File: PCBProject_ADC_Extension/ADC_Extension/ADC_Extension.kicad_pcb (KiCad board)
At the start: 2 copper layers, 279 parts, among them J1 Conn_01x20, J10 Conn_01x02, J11 Conn_01x02, J12 Conn_01x02, J13 Conn_01x02, J14 Conn_01x02, J15 Conn_01x02, J2 Conn_01x02, J3 Conn_01x02, J4 Conn_01x02, J5 Conn_01x02, J6 Conn_01x02, J7 Conn_01x02, J8 Conn_01x02, J9 Conn_01x02

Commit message: 布局50%请求援助
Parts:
- moved J11 8.34 mm to (67.0, 146.7), turned to -90 degrees
- moved J2 8.17 mm to (66.8, 77.7), turned to -90 degrees
- moved J15 7.18 mm to (118.0, 146.6), turned to -90 degrees
- moved J1 6.10 mm to (48.2, 86.9)
- moved ANALOGINPUT7 4.98 mm to (133.8, 108.3)
- moved C77 4.98 mm to (135.4, 130.3)
- moved C78 4.98 mm to (135.3, 126.8)
- moved D15 4.98 mm to (134.1, 119.4)
- moved D8 4.98 mm to (134.1, 104.8)
- moved R128 4.98 mm to (138.1, 122.4)
- moved R129 4.98 mm to (133.6, 133.7)
- moved R130 4.98 mm to (135.3, 123.2)
- moved R132 4.98 mm to (138.2, 127.4)
- moved R55 4.98 mm to (138.3, 102.3)
- moved R59 4.98 mm to (138.1, 97.2)
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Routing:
- net /ADC5: track 7.22 -> 125.2 mm, vias 0 -> 2
- net /ADD3: track 7.18 -> 123.3 mm, vias 0 -> 2
- net /ADD4: track 7.21 -> 58.3 mm
- net /ADB4: track 7.22 -> 52.4 mm, vias 0 -> 1
- net /AD_15: track 7.18 -> 42.1 mm
- net /IN-_9: track 0.00 -> 33.8 mm
- net /IN-_7: track 0.00 -> 33.0 mm
- net /IN-_13: track 0.00 -> 32.4 mm
- net /IN-_6: track 0.00 -> 31.4 mm
- net /IN-_12: track 0.00 -> 30.9 mm
- net /IN-_2: track 0.00 -> 30.2 mm
- net /ADC4: track 7.13 -> 36.4 mm
- net /ADC3: track 7.18 -> 36.4 mm, vias 0 -> 1
- net /IN-_3: track 0.00 -> 29.1 mm
- net /ADB5: track 7.21 -> 36.0 mm, vias 0 -> 1
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- added copper zone on In1.Cu, net AGND
- added copper zone on In2.Cu, net AGND
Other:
- copper layers 2 -> 4

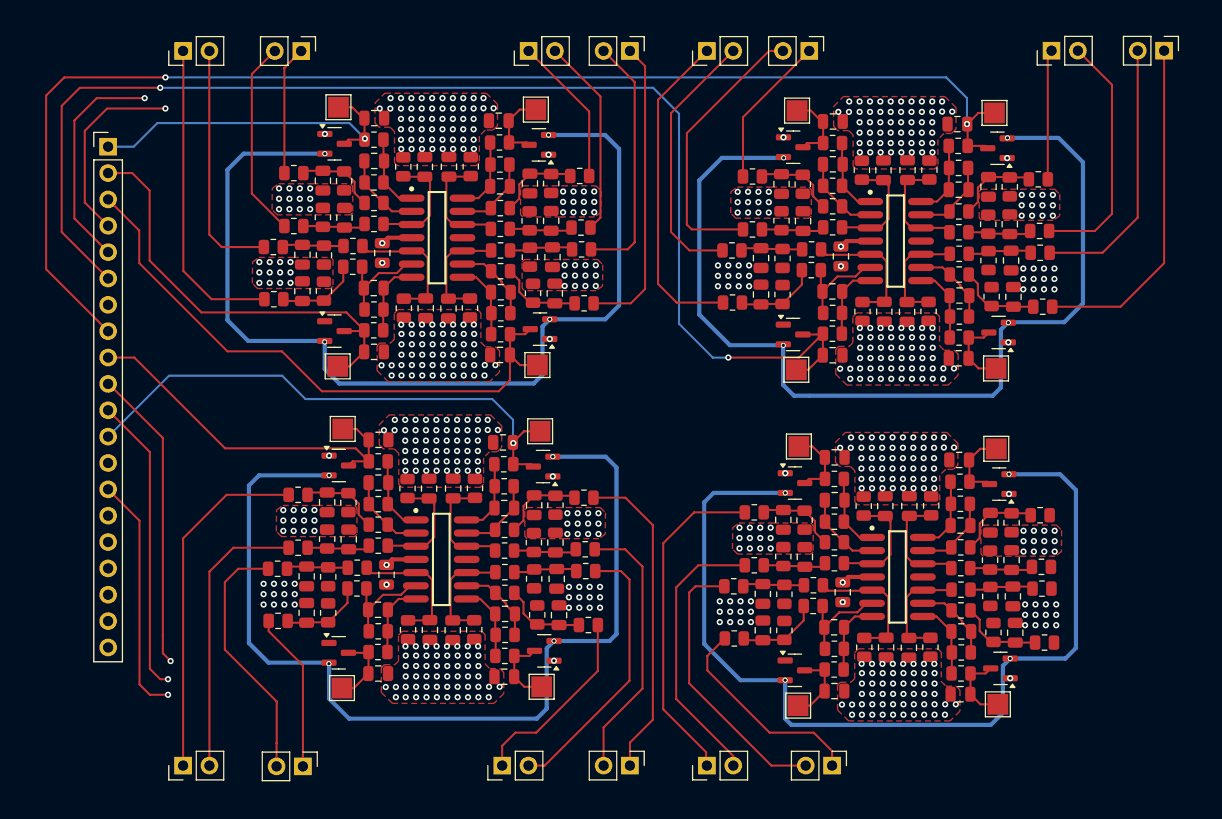
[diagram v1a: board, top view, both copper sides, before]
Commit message: 完成ADC拓展
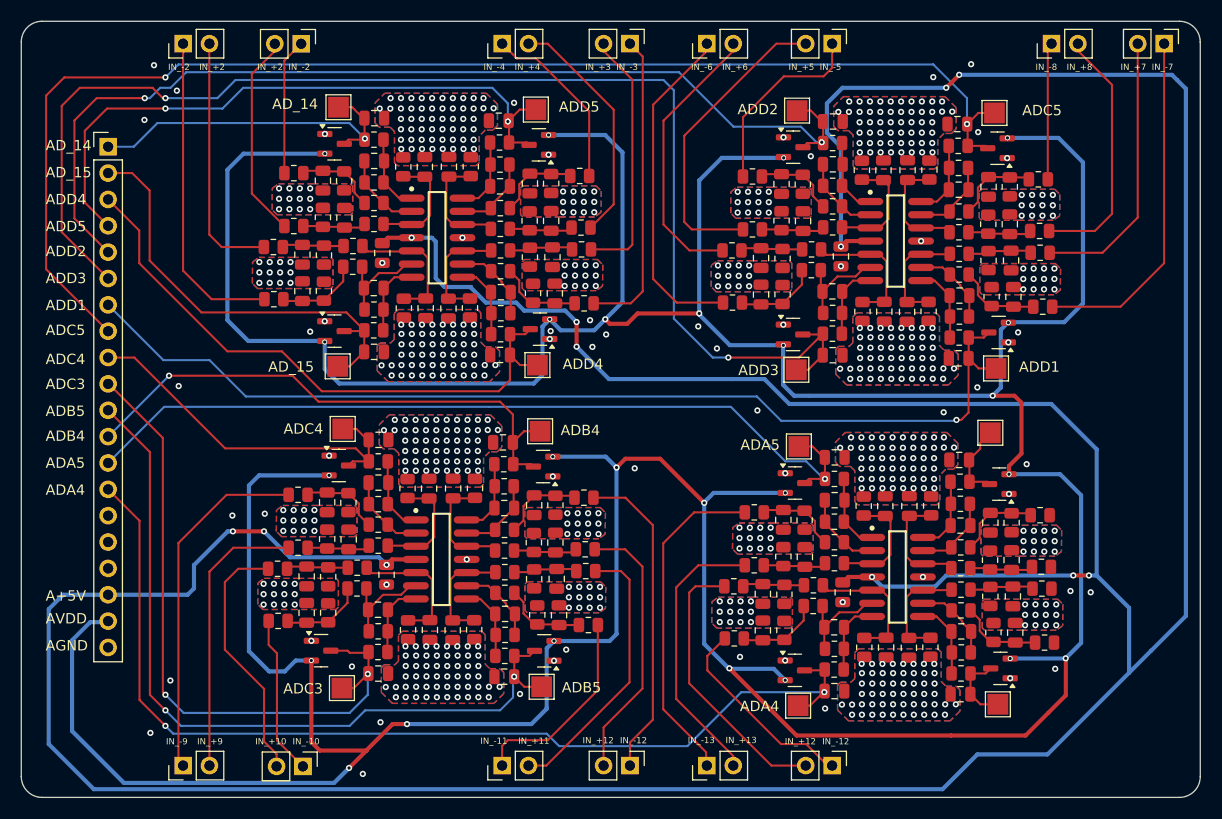
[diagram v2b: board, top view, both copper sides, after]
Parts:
- moved J5 2.64 mm to (86.2, 77.0)
- moved J6 2.31 mm to (118.0, 77.0)
- moved D10 1.71 mm to (68.8, 135.5)
- moved ANALOGINPUT16 1.65 mm to (133.2, 114.5)
- moved J3 0.70 mm to (55.5, 77.0)
- moved J4 0.70 mm to (98.5, 77.0)
- moved J7 0.70 mm to (105.9, 77.0)
- moved J2 0.70 mm to (66.8, 77.0)
- moved J8 0.67 mm to (150.0, 77.0)
- moved J9 0.67 mm to (139.2, 77.0)
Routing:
- net A+5V: track 12.2 -> 406.4 mm, vias 4 -> 12
- net /ADD1: track 7.21 -> 100.3 mm, vias 0 -> 1
- net AVDD: track 372.0 -> 464.7 mm, vias 16 -> 25
- net /ADA5: track 7.13 -> 81.3 mm, vias 0 -> 1
- net /ADD2: track 28.8 -> 97.9 mm, vias 1 -> 2
- net /ADA4: track 30.4 -> 98.7 mm, vias 1 -> 2
- net /ADB5: track 36.0 -> 75.7 mm, vias 1 -> 2
- net /ADD5: track 26.0 -> 62.2 mm, vias 1 -> 2
- net /ADC3: track 36.4 -> 64.2 mm, vias 1 -> 2
- net /IN+_4: track 19.2 -> 23.1 mm
- net /IN-_5: track 14.7 -> 18.6 mm
- net /IN-_4: track 14.5 -> 17.3 mm
- net /IN+_5: track 27.0 -> 29.6 mm
- net /ADD3: track 123.3 -> 125.8 mm
- net /IN-_2: track 30.2 -> 31.6 mm
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- added copper zone on B.Cu, net AGND
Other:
- board outline added: 113.6 x 74.8 mm
- board text added: "A+5V"
- board text added: "ADA4"
- board text added: "ADA5"
- board text added: "ADB4"
- board text added: "ADB5"
- board text added: "ADC3"
- board text added: "ADC4"
- board text added: "ADC5"
- board text added: "ADD1"
- board text added: "ADD2"
- board text added: "ADD3"
- board text added: "ADD4"
- board text added: "ADD5"
- board text added: "AD_14"
- board text added: "AD_15"
- board text added: "AGND"
- board text added: "AVDD"
- board text added: "IN_+10"
- board text added: "IN_+11"
- board text added: "IN_+12"
- board text added: "IN_+13"
- board text added: "IN_+2"
- board text added: "IN_+3"
- board text added: "IN_+4"
- board text added: "IN_+5"
- board text added: "IN_+6"
- board text added: "IN_+7"
- board text added: "IN_+8"
- board text added: "IN_+9"
- board text added: "IN_-10"
- board text added: "IN_-11"
- board text added: "IN_-12"
- board text added: "IN_-13"
- board text added: "IN_-2"
- board text added: "IN_-3"
- board text added: "IN_-4"
- board text added: "IN_-5"
- board text added: "IN_-6"
- board text added: "IN_-7"
- board text added: "IN_-8"
- board text added: "IN_-9"
